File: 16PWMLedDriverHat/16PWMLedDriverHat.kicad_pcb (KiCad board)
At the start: 2 copper layers, 65 x 56 mm, 22 parts, among them J0 RPi_GPIO, P1 C A0 A1 A2 A3 A4 A5 A6 A7, P2 C B0 B1 B2 B3 B4 B5 B6 B7, U1 PCA9685, U2 TBD62X83A, U3 TBD62X83A

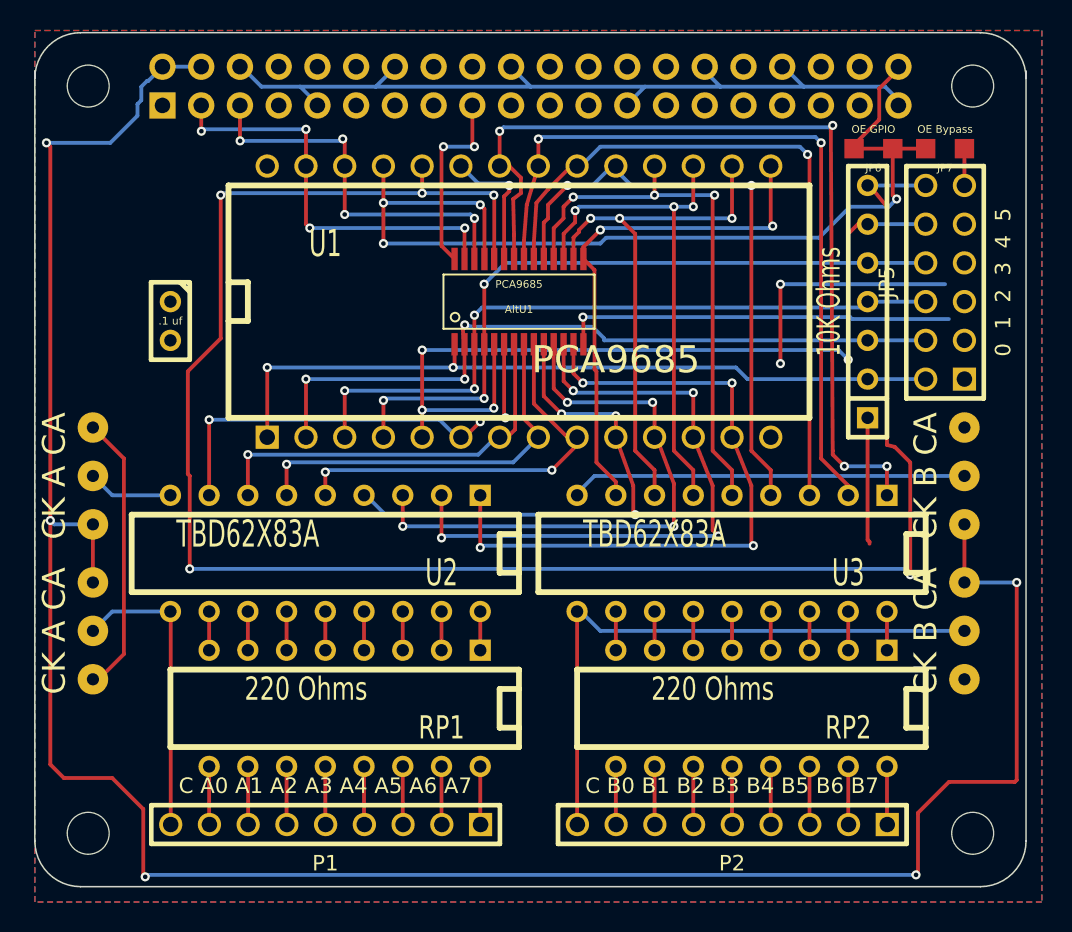
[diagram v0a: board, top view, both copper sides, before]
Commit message: Convert the 16PWM Led Drivers to use 12V for the LEDs.
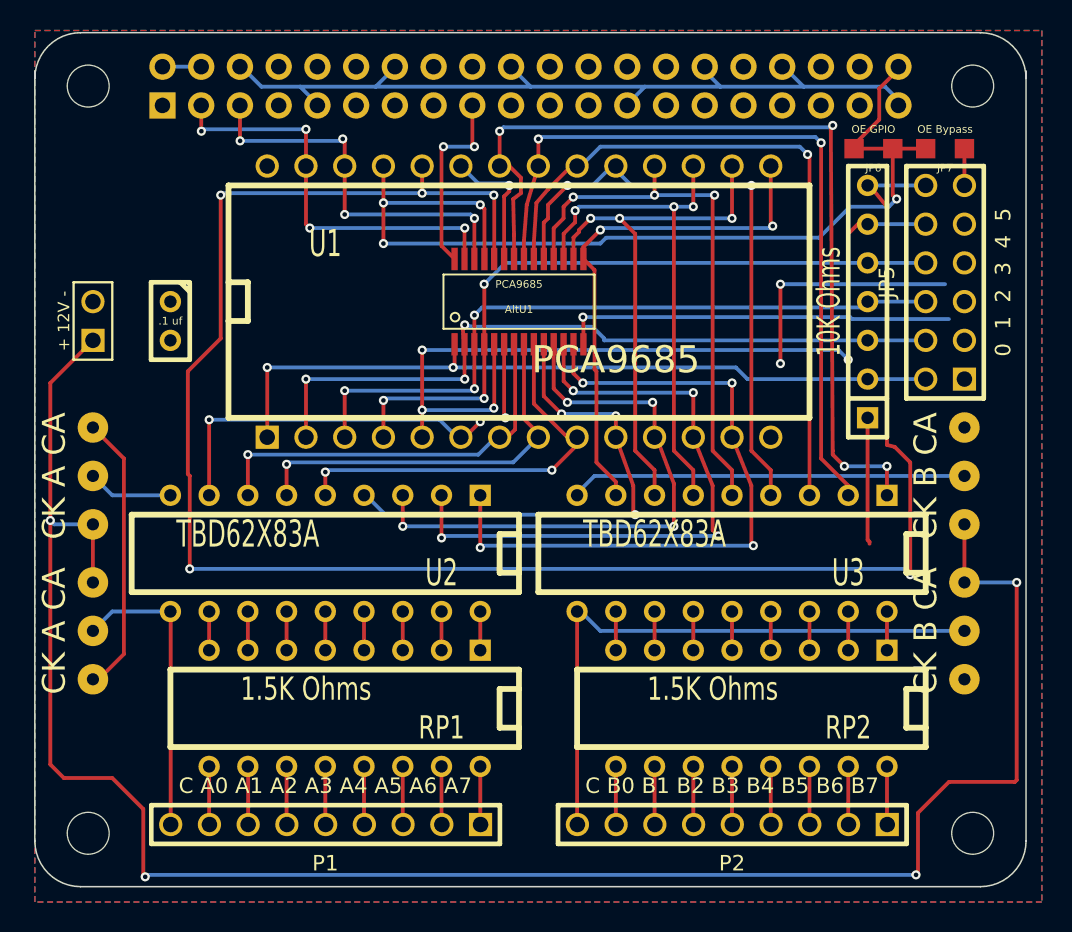
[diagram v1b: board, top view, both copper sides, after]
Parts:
- added T1: + 12V -, ScrewTerm2.54-2, F.Cu at (41.9, 50.8)
- RP1, RP2: value 220 Ohms -> 1.5K Ohms
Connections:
- JP1 pad 1: +5V -> +12V
- JP2 pad 3: +5V -> +12V
- JP3 pad 1: +5V -> +12V
- JP4 pad 3: +5V -> +12V
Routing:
- net +5V: track 154.8 -> 2.54 mm, vias 5 -> 0
- net +12V: track 0.00 -> 129.8 mm, vias 0 -> 4

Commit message: Remove unnecessary DIP from 16PWMLedDriverHat.
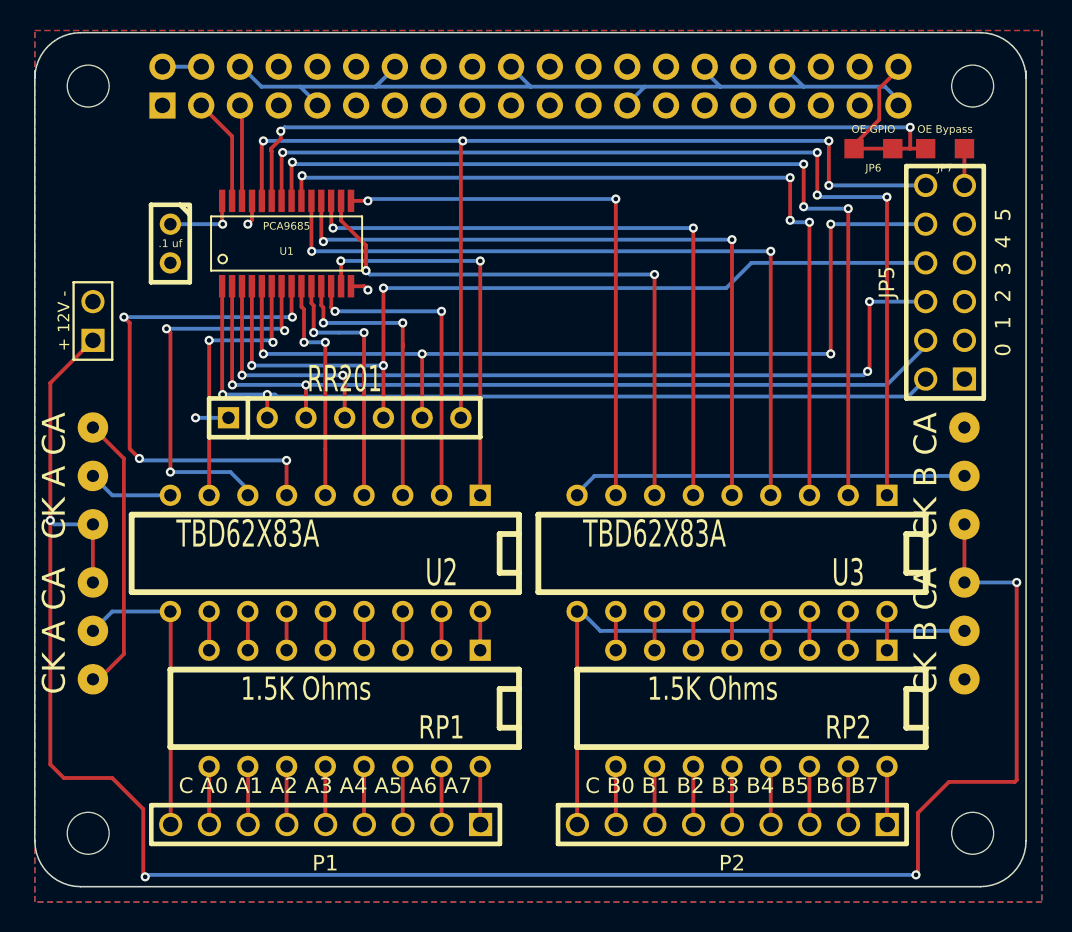
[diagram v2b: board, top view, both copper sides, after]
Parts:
- removed AltU1: PCA9685, tssop-28
- removed RR1: 10K Ohms, SIL-7
- added RR201: 10K Ohms, SIL-7, F.Cu at (58.4, 57.1)
- U1: footprint DIP-28__700 -> tssop-28
- moved U1 15.7 mm to (54.6, 45.7)
- moved C1 5.08 mm to (47.0, 45.7)
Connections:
- JP6 pad 2: N-0000070 (its old number) -> N-0000073
- JP7 pad 1: N-0000070 (its old number) -> N-0000073
- U1 pad 23: N-0000069 (its old number) -> N-0000073
- U1 pad 25: N-0000070 (its old number) -> GND
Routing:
- net N-0000084: track 127.5 -> 68.7 mm, vias 5 -> 4
- net N-0000070 (its old number): track 55.6 -> 0.00 mm, vias 4 -> 0
- net N-0000073: track 0.00 -> 49.8 mm, vias 0 -> 2
- net GND: track 101.9 -> 79.1 mm, vias 1 -> 2
- net N-00000108: track 42.0 -> 20.8 mm, vias 4 -> 2
- net /PCA9685 Driver/SDA: track 27.4 -> 7.10 mm, vias 4 -> 0
- net /PCA9685 Driver/SCL: track 25.4 -> 6.31 mm, vias 4 -> 0
- net N-00000113: track 38.1 -> 19.1 mm, vias 4 -> 2
- net N-00000118: track 44.9 -> 26.2 mm, vias 4 -> 2
- net N-00000109: track 33.7 -> 17.1 mm, vias 3 -> 2
- net (no net): track 16.0 -> 0.00 mm, vias 2 -> 0
- net +3.3V: track 20.9 -> 7.13 mm
- net N-0000071: track 46.1 -> 58.6 mm
- net N-0000061: track 30.2 -> 18.1 mm, vias 3 -> 2
- net N-0000096: track 26.9 -> 15.2 mm
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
